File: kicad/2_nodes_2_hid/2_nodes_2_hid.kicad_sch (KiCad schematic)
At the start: 14 parts

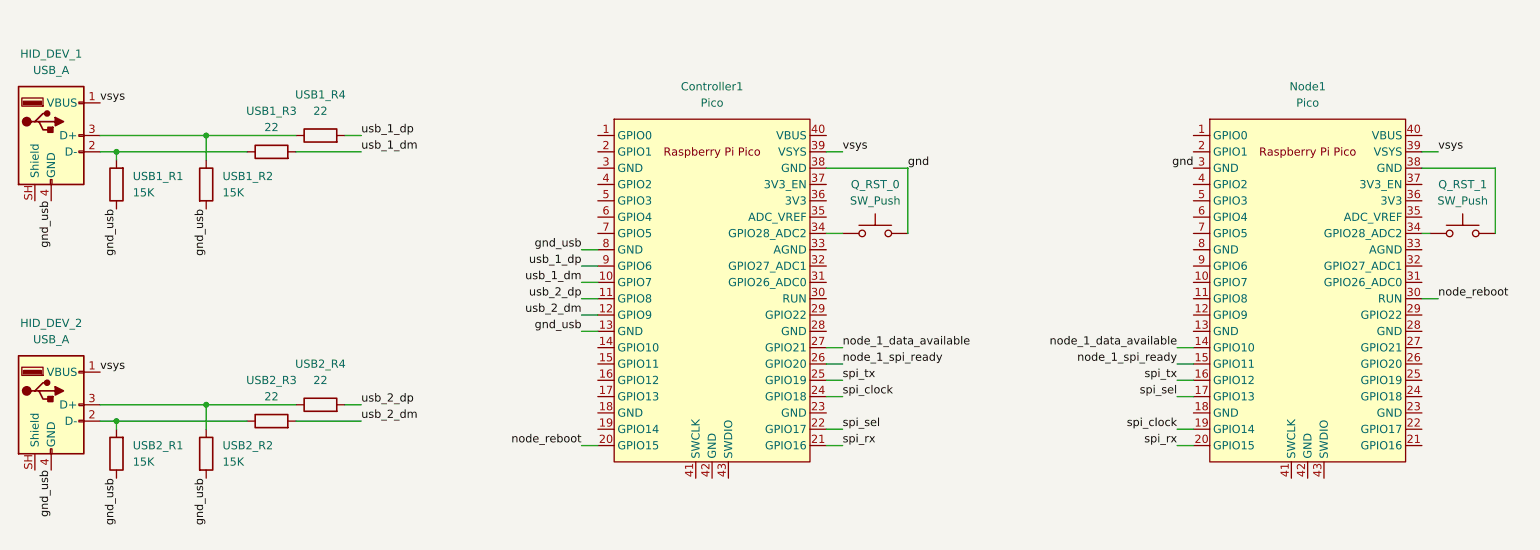
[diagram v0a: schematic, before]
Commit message: Update Kicad schematic, more compact design
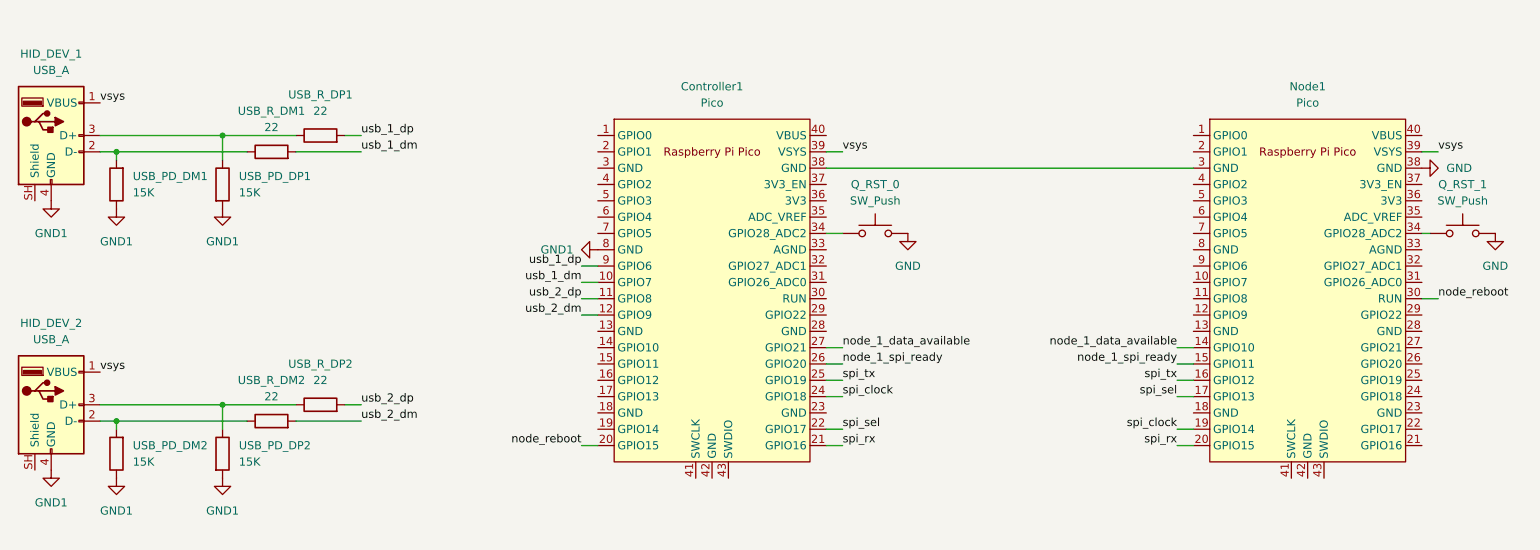
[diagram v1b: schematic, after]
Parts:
- renumbered USB1_R1 to USB_PD_DM1, USB2_R1 to USB_PD_DM2, USB1_R2 to USB_PD_DP1, USB2_R2 to USB_PD_DP2, USB1_R3 to USB_R_DM1, USB2_R3 to USB_R_DM2, USB1_R4 to USB_R_DP1, USB2_R4 to USB_R_DP2
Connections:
- net GND: now reaches Node1.38 (GND), Q_RST_1.2
- net GND: now also Q_RST_0.2
- net gnd: no longer names the net of Controller1.38 (GND), Node1.3 (GND)
- net gnd: no longer Q_RST_0.2
- net gnd_usb renamed GND1
- net GND1: no longer Controller1.13 (GND)
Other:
- moved on the sheet: USB_PD_DP1, USB_PD_DP2

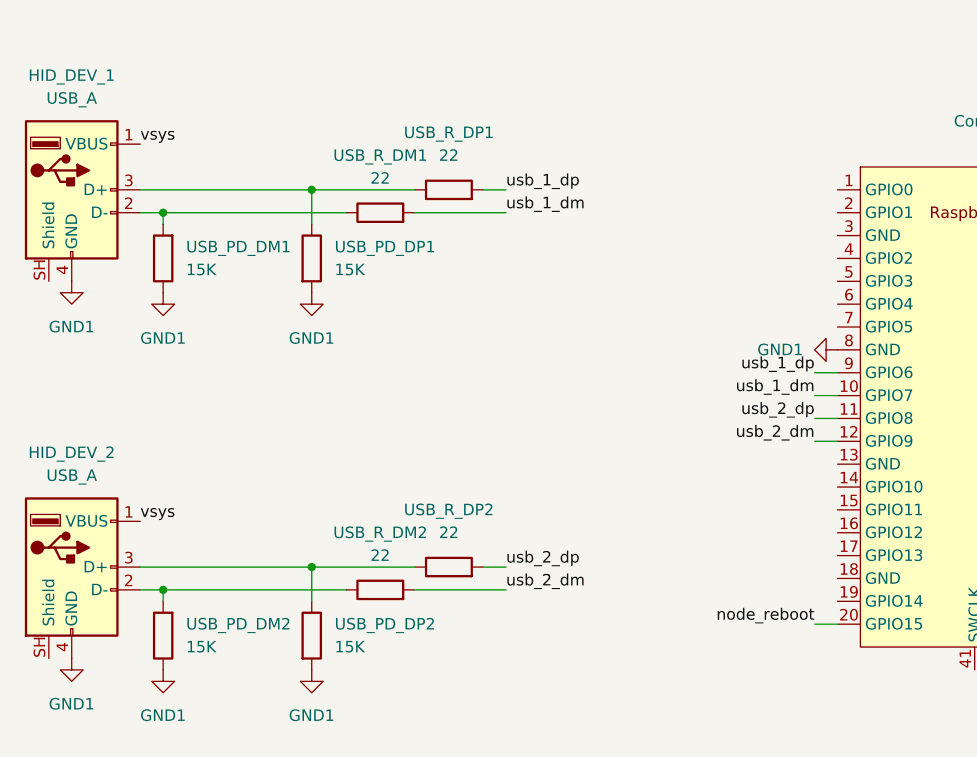
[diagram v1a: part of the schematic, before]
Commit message: Update PCB design, remove via on data tracks (inverted d+ and d-), add capacitor on usb ports
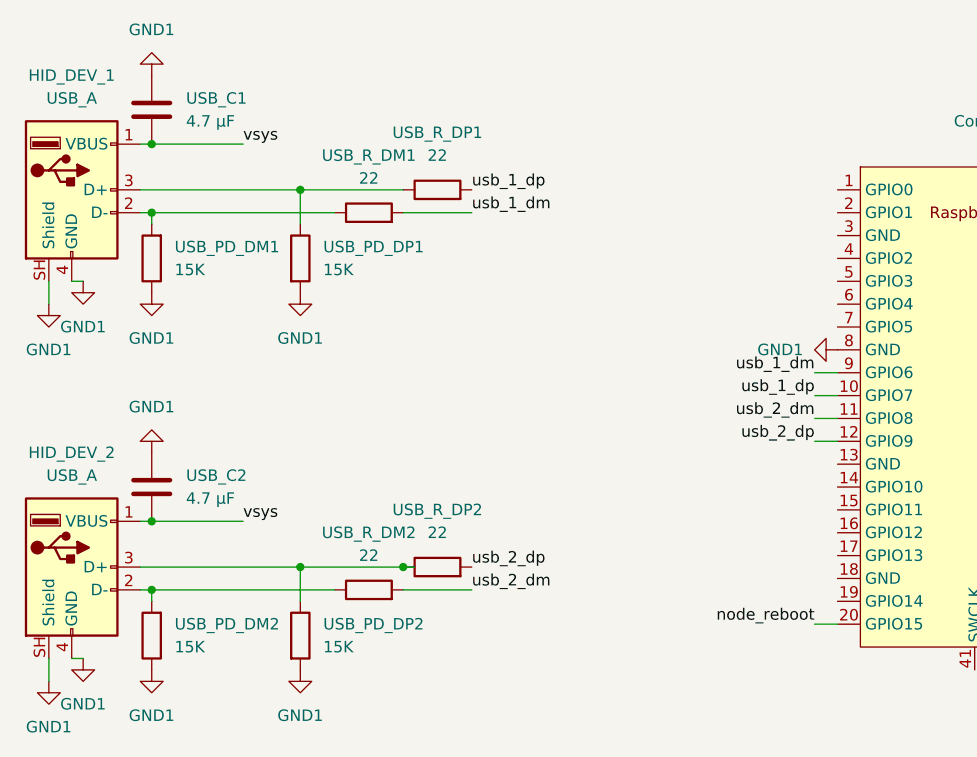
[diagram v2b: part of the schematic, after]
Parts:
- added USB_C1, USB_C2: 4.7 µF, Capacitor_SMD:C_1206_3216Metric_Pad1.33x1.80mm_HandSolder, symbol Device:C
- Q_RST_0, Q_RST_1: footprint Button_Switch_THT:SW_PUSH_1P1T_6x3.5mm_H4.3_APEM_MJTP1243 -> Button_Switch_SMD:SW_Push_1P1T_NO_E-Switch_TL3301NxxxxxG
- USB_PD_DM1, USB_PD_DM2, USB_PD_DP1, USB_PD_DP2, USB_R_DM1, USB_R_DM2, USB_R_DP1, USB_R_DP2: footprint Resistor_SMD:R_0603_1608Metric_Pad0.98x0.95mm_HandSolder -> Resistor_SMD:R_1206_3216Metric_Pad1.30x1.75mm_HandSolder
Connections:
- net GND1: now also HID_DEV_1.SH (Shield), HID_DEV_2.SH (Shield), USB_C1.1, USB_C2.1
- net usb_1_dm: now also Controller1.9 (GPIO6); no longer Controller1.10 (GPIO7)
- net usb_1_dp: now also Controller1.10 (GPIO7); no longer Controller1.9 (GPIO6)
- net usb_2_dm: now also Controller1.11 (GPIO8); no longer Controller1.12 (GPIO9)
- net usb_2_dp: now also Controller1.12 (GPIO9); no longer Controller1.11 (GPIO8)
- net vsys: now also USB_C1.2, USB_C2.2
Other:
- title: (none) -> KVM Switch - 2 Notes - 2 HID
- moved on the sheet: USB_PD_DM1, USB_PD_DM2, USB_PD_DP1, USB_PD_DP2, USB_R_DM1, USB_R_DM2, USB_R_DP1, USB_R_DP2

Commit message: Rework PCB design, increase size of the VSYS track and GND to handle 100mA at 5V
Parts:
- USB_C1, USB_C2: value 4.7 µF -> 10 µF
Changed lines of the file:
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@@
 			)
 		)
-		(property "Value" "4.7 µF"
+		(property "Value" "10 µF"
 			(at 35.56 88.8999 0)
 			(show_name no)
@@
 			)
 		)
-		(property "Value" "4.7 µF"
+		(property "Value" "10 µF"
 			(at 35.56 46.9899 0)
 			(show_name no)

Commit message: Rework PCB design, add ground plane, make sure d+ and d- track have same length and other various fix
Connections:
- net GND1 is gone; now on net GND: Controller1.8 (GND), HID_DEV_1.4 (GND), HID_DEV_1.SH (Shield), HID_DEV_2.4 (GND), HID_DEV_2.SH (Shield), USB_C1.1, USB_C2.1, USB_PD_DM1.1, USB_PD_DM2.1, USB_PD_DP1.2, USB_PD_DP2.2
- net GND: now also Controller1.13 (GND), Controller1.18 (GND), Controller1.23 (GND), Controller1.28 (GND), Controller1.3 (GND), Controller1.33 (AGND), Controller1.38 (GND), Node1.13 (GND), Node1.18 (GND), Node1.23 (GND), Node1.28 (GND), Node1.3 (GND), Node1.33 (AGND), Node1.8 (GND)
- net usb_1_dm renamed usb_1_d-
- net usb_1_dp renamed usb_1_d+
- net usb_2_dm renamed usb_2_d-
- net usb_2_dp renamed usb_2_d+
